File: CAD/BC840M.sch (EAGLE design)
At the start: 79 parts, among them J1 SM02B-SRSS-TB(LF)(SN), U2 BC840M, U3 LP5907MFX-3.3/NOPB, U4 LP5907MFX-3.3/NOPB, U5 ADS131M08IPBS, X1 ABM3B-8.000MHZ-B2-T, X2 FC-12M

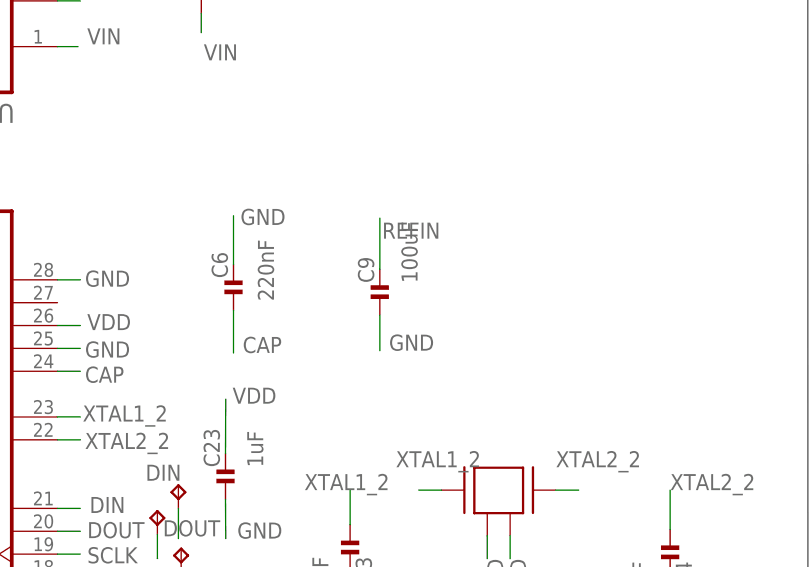
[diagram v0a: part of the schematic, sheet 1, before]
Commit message: removed cap on ads
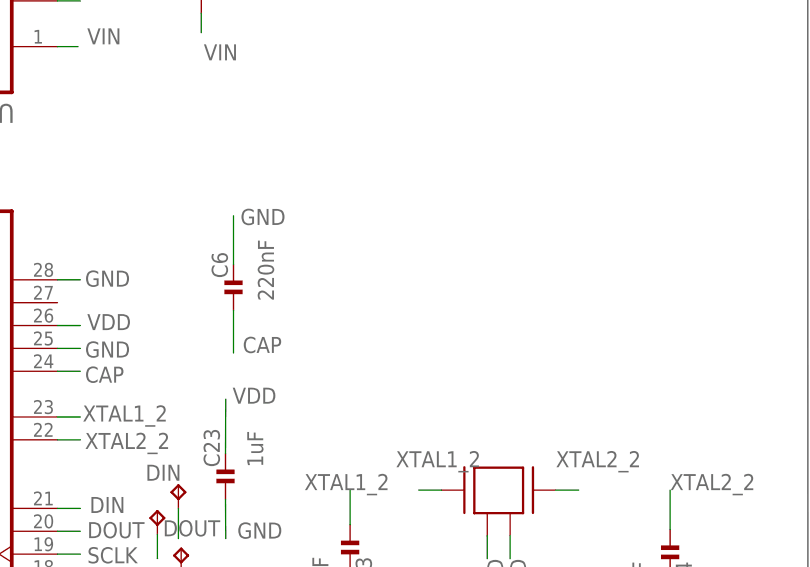
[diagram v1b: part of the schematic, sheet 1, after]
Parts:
- removed C9: 100uF, standardparts:CAPACITOR.0201
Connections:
- net GND: no longer C9.1
- net REFIN: no longer C9.2
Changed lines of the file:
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@@
 <part name="C8" library="standardparts" deviceset="CAPACITOR" device=".0201" value="1uF"/>
 <part name="U5" library="ADS131M08IPBS" deviceset="ADS131M08IPBS" device=""/>
-<part name="C9" library="standardparts" deviceset="CAPACITOR" device=".0201" value="100uF"/>
 <part name="P+1" library="supply1" library_urn="urn:adsk.eagle:library:371" deviceset="+5V" device=""/>
 <part name="SUPPLY3" library="supply2" library_urn="urn:adsk.eagle:library:372" deviceset="GND" device=""/>
@@
 <attribute name="VALUE" x="370.0526" y="20.3586" size="2.0828" layer="96" ratio="10" rot="SR0"/>
 </instance>
-<instance part="C9" gate="G$1" x="428.7266" y="83.947" smashed="yes" rot="R90">
-<attribute name="NAME" x="428.0916" y="84.963" size="1.778" layer="95" rot="R90"/>
-<attribute name="VALUE" x="432.9176" y="84.963" size="1.778" layer="96" rot="R90"/>
-</instance>
 <instance part="P+1" gate="1" x="119.0244" y="56.1848" smashed="yes">
 <attribute name="VALUE" x="116.4844" y="51.1048" size="1.778" layer="96" rot="R90"/>
@@
 <wire x1="412.4706" y1="87.0204" x2="412.4706" y2="92.4306" width="0.1524" layer="91"/>
 <label x="413.2326" y="91.4146" size="1.778" layer="95"/>
-</segment>
-<segment>
-<pinref part="C9" gate="G$1" pin="1"/>
-<wire x1="428.7266" y1="81.407" x2="428.7266" y2="77.4446" width="0.1524" layer="91"/>
-<label x="429.7426" y="77.4446" size="1.778" layer="95"/>
 </segment>
 <segment>
@@
 <label x="396.2146" y="31.7246" size="1.778" layer="95"/>
 </segment>
-<segment>
-<pinref part="C9" gate="G$1" pin="2"/>
-<wire x1="428.7266" y1="86.487" x2="428.7266" y2="92.1766" width="0.1524" layer="91"/>
-<label x="428.9806" y="89.8906" size="1.778" layer="95"/>
-</segment>
-</net>
+</net>

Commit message: updated
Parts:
- added SYNC: TPTP07R, testpad:TPTP07R
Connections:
- removed net CE: U$2.!CE
- removed net EN1: U$2.EN1
- removed net EN2: U$2.EN2
- removed net P27: U2.D6/P027
- removed net P6: U2.D7/P006
- net CHG: now also U2.D6/P027
- net GND: now also U$2.!CE, U$2.EN2, U$2.TMR
- net PGOOD: now also U2.D7/P006
- net SYNC/RESET: now also SYNC.TP
- net TMR: no longer U$2.TMR
- net VSWITCH: now also U$2.EN1
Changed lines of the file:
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@@
 <part name="NFC1" library="testpad" library_urn="urn:adsk.eagle:library:385" deviceset="TP" device="TP14SQ" package3d_urn="urn:adsk.eagle:package:27984/1" value="TPTP14SQ"/>
 <part name="NFC2" library="testpad" library_urn="urn:adsk.eagle:library:385" deviceset="TP" device="TP14SQ" package3d_urn="urn:adsk.eagle:package:27984/1" value="TPTP14SQ"/>
+<part name="SYNC" library="testpad" library_urn="urn:adsk.eagle:library:385" deviceset="TP" device="TP07R" package3d_urn="urn:adsk.eagle:package:27970/1" value="TPTP07R"/>
 </parts>
 <sheets>
@@
 <attribute name="TP_SIGNAL_NAME" x="226.568" y="21.463" size="1.778" layer="97"/>
 </instance>
+<instance part="SYNC" gate="G$1" x="399.1102" y="45.2374" smashed="yes">
+<attribute name="TP_SIGNAL_NAME" x="400.3802" y="43.9674" size="1.778" layer="97"/>
+</instance>
 </instances>
 <busses>
@@
 <wire x1="252.1712" y1="115.0112" x2="252.1712" y2="110.6932" width="0.1524" layer="91"/>
 </segment>
+<segment>
+<pinref part="U$2" gate="G$1" pin="TMR"/>
+<wire x1="48.1584" y1="37.6428" x2="44.6278" y2="37.6428" width="0.1524" layer="91"/>
+<label x="38.5826" y="37.0586" size="1.778" layer="95"/>
+</segment>
+<segment>
+<pinref part="U$2" gate="G$1" pin="!CE"/>
+<wire x1="48.1584" y1="83.3628" x2="44.45" y2="83.3628" width="0.1524" layer="91"/>
+<label x="43.3578" y="84.0486" size="1.778" layer="95" rot="R180"/>
+</segment>
+<segment>
+<pinref part="U$2" gate="G$1" pin="EN2"/>
+<wire x1="48.1584" y1="57.9628" x2="44.704" y2="57.9628" width="0.1524" layer="91"/>
+<wire x1="44.704" y1="57.9628" x2="44.704" y2="57.912" width="0.1524" layer="91"/>
+<label x="43.8658" y="58.5978" size="1.778" layer="95" rot="R180"/>
+</segment>
 </net>
 <net name="XTAL2_2" class="0">
@@
 <wire x1="207.0844" y1="31.1404" x2="207.0608" y2="31.1404" width="0.1524" layer="91"/>
 <label x="208.2292" y="15.0114" size="1.778" layer="95" rot="R90"/>
+</segment>
+<segment>
+<pinref part="SYNC" gate="G$1" pin="TP"/>
+<wire x1="399.1102" y1="42.6974" x2="399.1102" y2="40.513" width="0.1524" layer="91"/>
+<label x="399.2372" y="40.8178" size="1.778" layer="95"/>
 </segment>
 </net>
@@
 </segment>
 </net>
-<net name="P27" class="0">
-<segment>
-<pinref part="U2" gate="G$1" pin="D6/P027"/>
-<wire x1="211.0844" y1="35.3002" x2="211.0844" y2="31.1658" width="0.1524" layer="91"/>
-<wire x1="211.0844" y1="31.1658" x2="210.9724" y2="31.1658" width="0.1524" layer="91"/>
-<label x="212.0138" y="26.0858" size="1.778" layer="95" rot="R90"/>
-</segment>
-</net>
-<net name="P6" class="0">
-<segment>
-<pinref part="U2" gate="G$1" pin="D7/P006"/>
-<wire x1="213.0844" y1="35.3002" x2="213.0844" y2="31.115" width="0.1524" layer="91"/>
-<wire x1="213.0844" y1="31.115" x2="213.106" y2="31.115" width="0.1524" layer="91"/>
-<label x="213.995" y="27.6098" size="1.778" layer="95" rot="R90"/>
-</segment>
-</net>
 <net name="P106" class="0">
 <segment>
@@
 </segment>
 </net>
-<net name="CE" class="0">
-<segment>
-<pinref part="U$2" gate="G$1" pin="!CE"/>
-<wire x1="48.1584" y1="83.3628" x2="44.45" y2="83.3628" width="0.1524" layer="91"/>
-<label x="43.3578" y="84.0486" size="1.778" layer="95" rot="R180"/>
-</segment>
-</net>
 <net name="N$67" class="0">
 <segment>
@@
 <wire x1="48.1584" y1="65.5828" x2="44.6786" y2="65.5828" width="0.1524" layer="91"/>
 <wire x1="44.6786" y1="65.5828" x2="44.6786" y2="65.5574" width="0.1524" layer="91"/>
-</segment>
-</net>
-<net name="EN1" class="0">
-<segment>
-<pinref part="U$2" gate="G$1" pin="EN1"/>
-<wire x1="48.1584" y1="60.5028" x2="44.7548" y2="60.5028" width="0.1524" layer="91"/>
-<label x="43.7896" y="61.4934" size="1.778" layer="95" rot="R180"/>
-</segment>
-</net>
-<net name="EN2" class="0">
-<segment>
-<pinref part="U$2" gate="G$1" pin="EN2"/>
-<wire x1="48.1584" y1="57.9628" x2="44.704" y2="57.9628" width="0.1524" layer="91"/>
-<wire x1="44.704" y1="57.9628" x2="44.704" y2="57.912" width="0.1524" layer="91"/>
-<label x="43.8658" y="58.5978" size="1.778" layer="95" rot="R180"/>
 </segment>
 </net>
@@
 <label x="33.274" y="40.259" size="1.778" layer="95" rot="R180"/>
 </segment>
-<segment>
-<pinref part="U$2" gate="G$1" pin="TMR"/>
-<wire x1="48.1584" y1="37.6428" x2="44.6278" y2="37.6428" width="0.1524" layer="91"/>
-<label x="38.5826" y="37.0586" size="1.778" layer="95"/>
-</segment>
 </net>
 <net name="ILM" class="0">
@@
 <label x="37.6682" y="74.0918" size="1.778" layer="95"/>
 </segment>
+<segment>
+<pinref part="U2" gate="G$1" pin="D7/P006"/>
+<wire x1="213.0844" y1="35.3002" x2="213.0844" y2="31.115" width="0.1524" layer="91"/>
+<wire x1="213.0844" y1="31.115" x2="213.106" y2="31.115" width="0.1524" layer="91"/>
+<label x="214.0204" y="21.4122" size="1.778" layer="95" rot="R90"/>
+</segment>
 </net>
 <net name="CHG" class="0">
@@
 <label x="37.8968" y="78.9432" size="1.778" layer="95"/>
 </segment>
+<segment>
+<pinref part="U2" gate="G$1" pin="D6/P027"/>
+<wire x1="211.0844" y1="35.3002" x2="211.0844" y2="31.1658" width="0.1524" layer="91"/>
+<label x="212.0392" y="25.2984" size="1.778" layer="95" rot="R90"/>
+</segment>
 </net>
 <net name="BAT" class="0">
@@
 <pinref part="U$2" gate="G$1" pin="BAT@2"/>
 <wire x1="48.1584" y1="68.1228" x2="44.577" y2="68.1228" width="0.1524" layer="91"/>
-<label x="43.1038" y="66.929" size="1.778" layer="95" rot="R90"/>
+<label x="44.3738" y="69.3928" size="1.778" layer="95" rot="R180"/>
 </segment>
 <segment>
@@
 <label x="98.7552" y="101.0666" size="1.778" layer="95" rot="R270"/>
 </segment>
+<segment>
+<pinref part="U$2" gate="G$1" pin="EN1"/>
+<wire x1="48.1584" y1="60.5028" x2="44.7548" y2="60.5028" width="0.1524" layer="91"/>
+<label x="43.7896" y="61.4934" size="1.778" layer="95" rot="R180"/>
+</segment>
 </net>
 <net name="+5V_ISO" class="0">
@@
 <wire x1="48.1584" y1="90.9828" x2="44.1198" y2="90.9828" width="0.1524" layer="91"/>
 <wire x1="44.1198" y1="90.9828" x2="44.1198" y2="91.1098" width="0.1524" layer="91"/>
-<label x="42.9768" y="86.3854" size="1.778" layer="95" rot="R90"/>
-</segment>
-</net>
+<label x="46.4058" y="93.7768" size="1.778" layer="95" rot="R180"/>
+</segment>
+</net>

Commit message: more tweaks
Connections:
- net VDD: now also R25.1, R25.2
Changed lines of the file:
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@@
 <label x="412.369" y="71.5518" size="1.778" layer="95"/>
+</segment>
+<segment>
+<pinref part="R25" gate="G$1" pin="1"/>
+<wire x1="144.5514" y1="56.2356" x2="140.0302" y2="56.2356" width="0.1524" layer="91"/>
+<label x="134.112" y="56.3626" size="1.778" layer="95"/>
+</segment>
+<segment>
+<pinref part="R25" gate="G$1" pin="2"/>
+<wire x1="149.6314" y1="56.2356" x2="153.162" y2="56.2356" width="0.1524" layer="91"/>
+<wire x1="153.162" y1="56.2356" x2="153.162" y2="56.3118" width="0.1524" layer="91"/>
+<label x="152.4762" y="57.023" size="1.778" layer="95"/>
 </segment>
 </net>

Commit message: latest
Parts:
- added C26, C9: 4.7uF, standardparts:CAPACITOR.0201
- added C27: 0.1uF, standardparts:CAPACITOR.0201
- added R28, R29: 10kΩ, standardparts:RESISTOR.0402
- added SJ2: (no value), jumper:SJ
- R1: value 46.4kΩ -> 10kΩ
- R3: device standardparts:RESISTOR.0201 -> standardparts:RESISTOR.0603; SPICEPREFIX (none) -> R
- R4: device standardparts:RESISTOR.0201 -> standardparts:RESISTOR.0603
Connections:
- net P4 renamed CUR_DETECT
- net XTAL1_2 renamed CLKIN
- removed net N$67: U$2.BAT@3
- removed net REFIN: U5.REFIN
- removed net TD: U$2.TD
- removed net TMR: R1.1
- removed net VDDH: U2.A7/VDDH
- removed net XTAL2_2: C4.1, U5.XTAL2, X1.3
- new net CLKOUT: C4.1, JP3.1, U5.XTAL2, X1.3
- net +5V: now also C9.2
- net +5V_ISO: now also C26.2, C27.2
- net AVDD: now also SJ2.1, SJ2.2
- net BAT: now also U$2.BAT@3
- net CHG: now also R29.2
- net DIN: now also JP3.19
- net DOUT: now also JP3.17
- net GND: now also C26.1, C27.1, C9.1, JP3.5, R1.1, U$2.TD, U5.REFIN; no longer R1.2
- net P101: now also JP2.8
- net P104: now also JP2.10
- net P106: now also JP3.11
- net P107: now also JP2.14
- net P108: now also JP2.13
- net P109: now also JP2.15
- net P11: now also JP2.5
- net P110: now also JP3.18
- net P111: now also JP3.4
- net P113: now also JP3.6
- net P114: now also JP3.8
- net P12: now also JP2.9
- net P14: now also JP2.1
- net P15: now also JP2.2
- net P17: now also JP2.3
- net P19: now also JP2.19
- net P2: now also JP3.14
- net P21: now also JP2.12
- net P22: now also JP2.6
- net P23: now also JP3.13
- net P24: now also JP3.20
- net P25: now also JP2.4
- net P28: now also JP3.2
- net P29: now also JP3.16
- net P3: now also JP3.9
- net P30: now also JP3.7
- net P31: now also JP3.12
- net P5: now also JP3.10
- net P7: now also JP2.11
- net P8: now also JP2.7
- net PGOOD: now also R28.2
- net RESET: now also JP2.17
- net SCLK: now also JP3.15
- net SWDCLK: now also JP2.18
- net SWDIO: now also JP2.16
- net SWO: now also JP2.20
- net TS: now also R1.2
- net VDD: now also R28.1, R29.1, U2.A7/VDDH
- net VIN: now also JP3.3
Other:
- moved on the sheet: C14, C19, J1, JP2, JP3, R1, R2, R25, R4

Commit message: touchups
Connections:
- net VDD: now also JP3.3
- net VIN: no longer JP3.3
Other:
- note added: "BC840M"
- note added: "Common LDO"
- note added: "Low Pass Filters"
- moved on the sheet: C1, C10, C11, C12, C13, C14, C15, C16, C17, C18, C19, C2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

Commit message: _
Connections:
- removed net N$76: U$2.OUT@11
- net VSWITCH: now also U$2.OUT@11
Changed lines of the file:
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@@
-</segment>
-</net>
-<net name="N$76" class="0">
-<segment>
-<pinref part="U$2" gate="G$1" pin="OUT@11"/>
-<wire x1="86.1822" y1="154.305" x2="88.0872" y2="154.305" width="0.1524" layer="91"/>
-<wire x1="88.0872" y1="154.305" x2="88.0872" y2="154.2796" width="0.1524" layer="91"/>
 </segment>
 </net>
@@
 <label x="46.2534" y="127.3556" size="1.778" layer="95" rot="R180"/>
 </segment>
-</net>
+<segment>
+<pinref part="U$2" gate="G$1" pin="OUT@11"/>
+<wire x1="86.1822" y1="154.305" x2="88.0872" y2="154.305" width="0.1524" layer="91"/>
+<wire x1="88.0872" y1="154.305" x2="88.0872" y2="154.2796" width="0.1524" layer="91"/>
+<label x="82.6516" y="151.1046" size="1.778" layer="95"/>
+</segment>
+</net>

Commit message: latest
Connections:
- new net AVDD1: SJ2.1, U4.OUT
- new net TMR: U$2.TMR
- net AVDD: no longer SJ2.1, U4.OUT
- net GND: now also U$2.EN1; no longer U$2.EN2, U$2.TMR
- net P11: now also JP2.7; no longer JP2.5
- net P8: now also JP2.5; no longer JP2.7
- net VSWITCH: now also U$2.EN2; no longer U$2.EN1
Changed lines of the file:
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@@
-</segment>
-<segment>
-<pinref part="U$2" gate="G$1" pin="TMR"/>
-<wire x1="50.6222" y1="103.505" x2="47.0916" y2="103.505" width="0.1524" layer="91"/>
-<label x="43.2562" y="101.2444" size="1.778" layer="95"/>
 </segment>
 <segment>
@@
 <wire x1="50.6222" y1="149.225" x2="46.9138" y2="149.225" width="0.1524" layer="91"/>
 <label x="45.8216" y="149.9108" size="1.778" layer="95" rot="R180"/>
-</segment>
-<segment>
-<pinref part="U$2" gate="G$1" pin="EN2"/>
-<wire x1="50.6222" y1="123.825" x2="47.1678" y2="123.825" width="0.1524" layer="91"/>
-<wire x1="47.1678" y1="123.825" x2="47.1678" y2="123.7742" width="0.1524" layer="91"/>
-<label x="46.3296" y="124.46" size="1.778" layer="95" rot="R180"/>
 </segment>
 <segment>
@@
 <label x="283.9466" y="73.3298" size="1.778" layer="95"/>
 </segment>
+<segment>
+<pinref part="U$2" gate="G$1" pin="EN1"/>
+<wire x1="50.6222" y1="126.365" x2="47.2186" y2="126.365" width="0.1524" layer="91"/>
+<label x="46.2534" y="127.3556" size="1.778" layer="95" rot="R180"/>
+</segment>
 </net>
 <net name="CLKIN" class="0">
@@
 </segment>
 <segment>
-<pinref part="U4" gate="G$1" pin="OUT"/>
-<wire x1="362.839" y1="190.6778" x2="360.807" y2="190.6778" width="0.1524" layer="91"/>
-<label x="358.775" y="188.3918" size="1.778" layer="95"/>
-</segment>
-<segment>
 <pinref part="C8" gate="G$1" pin="1"/>
-<wire x1="350.8502" y1="194.3354" x2="350.901" y2="190.4238" width="0.1524" layer="91"/>
+<wire x1="350.8502" y1="194.3354" x2="350.8502" y2="190.4238" width="0.1524" layer="91"/>
 <label x="350.901" y="189.4078" size="1.778" layer="95"/>
 </segment>
@@
 <wire x1="343.8652" y1="201.5744" x2="343.8652" y2="204.1144" width="0.1524" layer="91"/>
 <label x="343.154" y="203.4794" size="1.778" layer="95" rot="R90"/>
-</segment>
-<segment>
-<pinref part="SJ2" gate="1" pin="1"/>
-<wire x1="343.8652" y1="191.4144" x2="343.8652" y2="189.0522" width="0.1524" layer="91"/>
-<wire x1="343.8652" y1="189.0522" x2="343.8144" y2="189.0522" width="0.1524" layer="91"/>
-<label x="343.0778" y="184.9628" size="1.778" layer="95" rot="R90"/>
 </segment>
 </net>
@@
 </segment>
 <segment>
-<pinref part="JP2" gate="A" pin="7"/>
-<wire x1="161.29" y1="80.4418" x2="167.5638" y2="80.4418" width="0.1524" layer="91"/>
-<label x="167.6654" y="79.7306" size="1.778" layer="95"/>
+<pinref part="JP2" gate="A" pin="5"/>
+<wire x1="161.29" y1="77.9018" x2="167.767" y2="77.9018" width="0.1524" layer="91"/>
+<label x="167.9956" y="77.2414" size="1.778" layer="95"/>
 </segment>
 </net>
@@
 </segment>
 <segment>
-<pinref part="JP2" gate="A" pin="5"/>
-<wire x1="161.29" y1="77.9018" x2="167.767" y2="77.9018" width="0.1524" layer="91"/>
-<label x="167.9956" y="77.2414" size="1.778" layer="95"/>
+<pinref part="JP2" gate="A" pin="7"/>
+<wire x1="161.29" y1="80.4418" x2="167.5638" y2="80.4418" width="0.1524" layer="91"/>
+<label x="167.6654" y="79.7306" size="1.778" layer="95"/>
 </segment>
 </net>
@@
 </segment>
 <segment>
-<pinref part="U$2" gate="G$1" pin="EN1"/>
-<wire x1="50.6222" y1="126.365" x2="47.2186" y2="126.365" width="0.1524" layer="91"/>
-<label x="46.2534" y="127.3556" size="1.778" layer="95" rot="R180"/>
-</segment>
-<segment>
 <pinref part="U$2" gate="G$1" pin="OUT@11"/>
 <wire x1="86.1822" y1="154.305" x2="88.0872" y2="154.305" width="0.1524" layer="91"/>
 <wire x1="88.0872" y1="154.305" x2="88.0872" y2="154.2796" width="0.1524" layer="91"/>
 <label x="82.6516" y="151.1046" size="1.778" layer="95"/>
+</segment>
+<segment>
+<pinref part="U$2" gate="G$1" pin="EN2"/>
+<wire x1="50.6222" y1="123.825" x2="47.1678" y2="123.825" width="0.1524" layer="91"/>
+<wire x1="47.1678" y1="123.825" x2="47.1678" y2="123.7742" width="0.1524" layer="91"/>
+<label x="46.3296" y="124.46" size="1.778" layer="95" rot="R180"/>
 </segment>
 </net>
@@
 </segment>
 </net>
+<net name="AVDD1" class="0">
+<segment>
+<pinref part="SJ2" gate="1" pin="1"/>
+<wire x1="343.8652" y1="191.4144" x2="343.8652" y2="189.0522" width="0.1524" layer="91"/>
+<label x="343.0778" y="184.9628" size="1.778" layer="95" rot="R90"/>
+</segment>
+<segment>
+<pinref part="U4" gate="G$1" pin="OUT"/>
+<wire x1="362.839" y1="190.6778" x2="360.3752" y2="190.6778" width="0.1524" layer="91"/>
+<label x="358.775" y="188.3918" size="1.778" layer="95"/>
+</segment>
+</net>
+<net name="TMR" class="0">
+<segment>
+<pinref part="U$2" gate="G$1" pin="TMR"/>
+<wire x1="50.6222" y1="103.505" x2="47.3456" y2="103.505" width="0.1524" layer="91"/>
+<wire x1="47.3456" y1="103.505" x2="47.3456" y2="103.4796" width="0.1524" layer="91"/>
+<label x="44.2976" y="103.7844" size="1.778" layer="95"/>
+</segment>
+</net>

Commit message: still need to add TVS diodes
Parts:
- added R30, R31: 100kΩ, standardparts:RESISTOR.0402
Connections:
- net CS: now also R31.1
- net DOUT: now also R30.1
- net GND: now also R30.2
- net VDD: now also R31.2
